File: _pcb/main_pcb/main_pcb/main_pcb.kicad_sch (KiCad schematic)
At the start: 1 part, among them U1 Pico

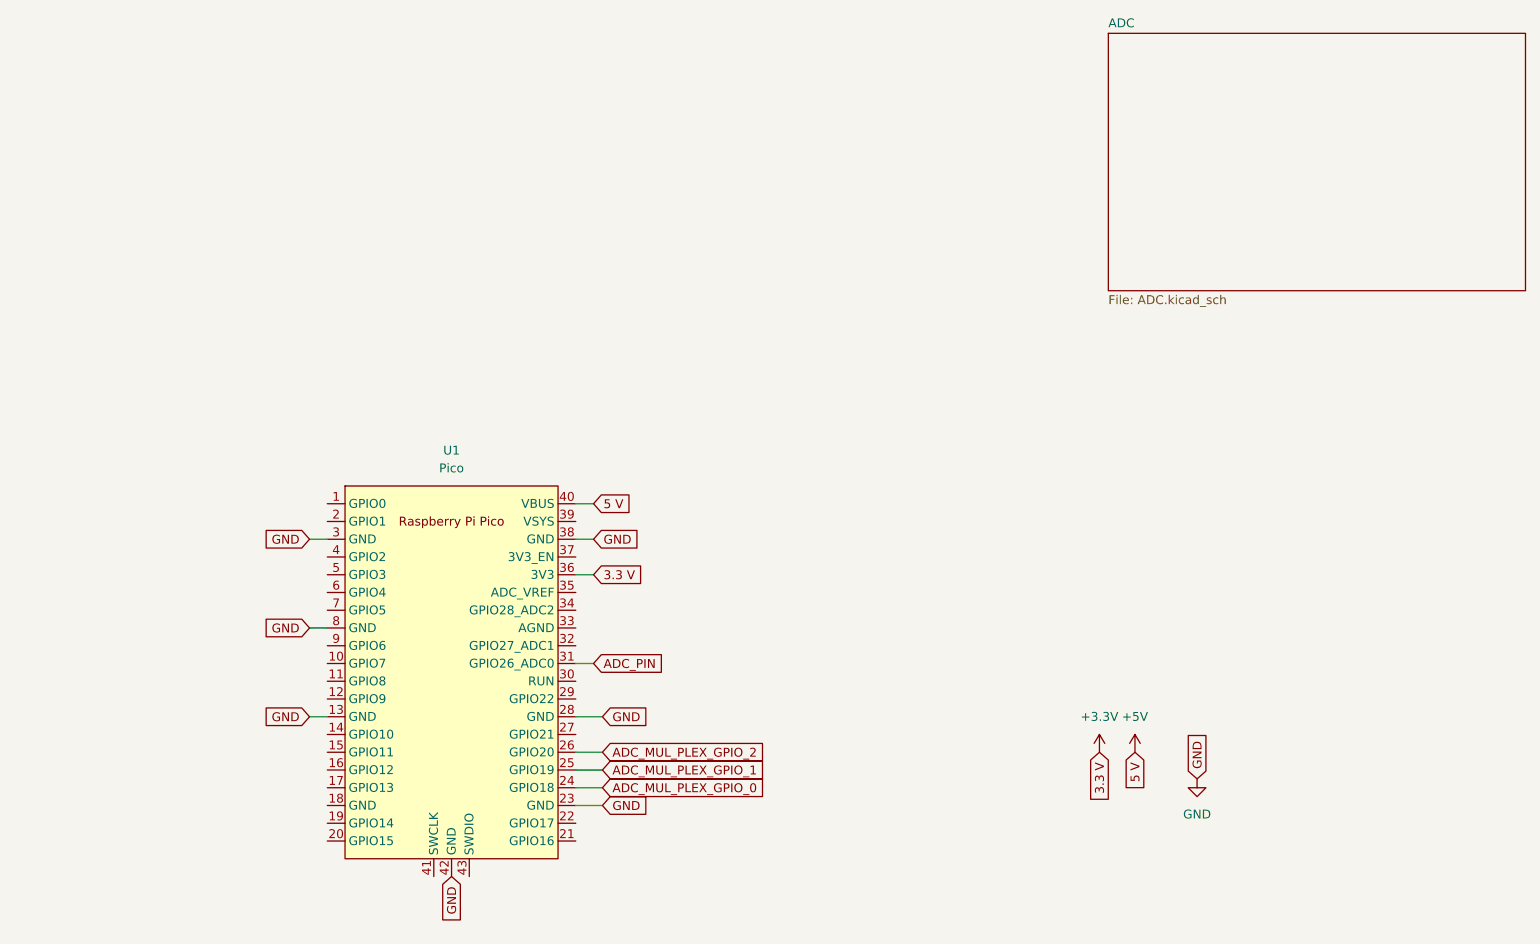
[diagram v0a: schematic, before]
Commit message: added io expander and rotSW only ws2812 missing
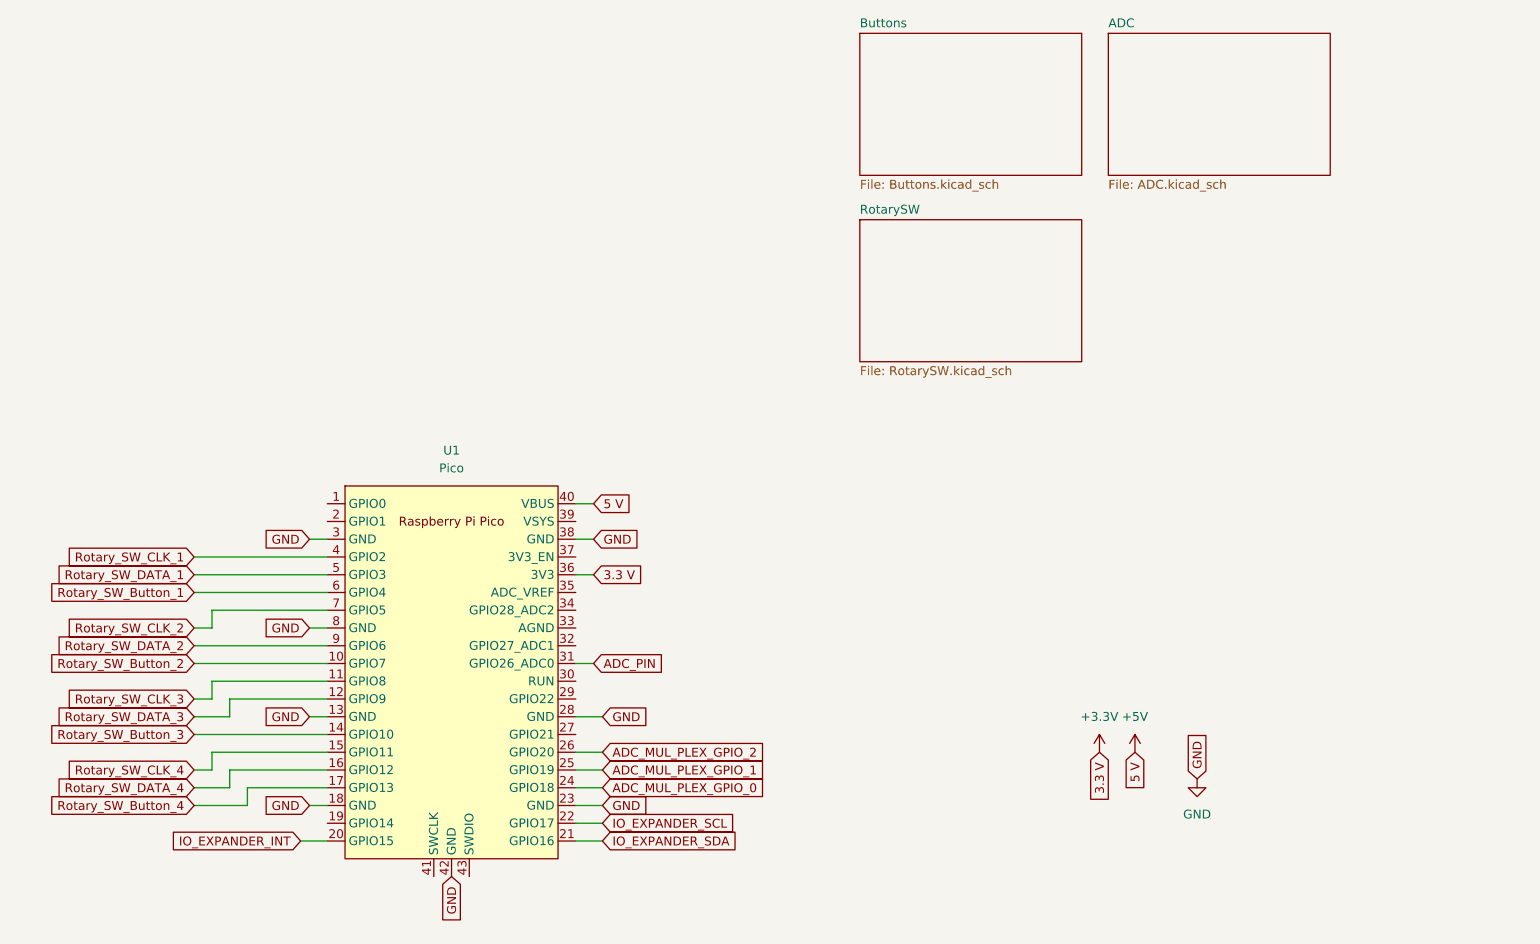
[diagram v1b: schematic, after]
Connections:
- net GND: now also U1.18 (GND)
- net Rotary_SW_Button_2: now reaches U1.10 (GPIO7)
- net Rotary_SW_CLK_3: now reaches U1.11 (GPIO8)
- net Rotary_SW_DATA_3: now reaches U1.12 (GPIO9)
- net Rotary_SW_Button_3: now reaches U1.14 (GPIO10)
- net Rotary_SW_CLK_4: now reaches U1.15 (GPIO11)
- net Rotary_SW_DATA_4: now reaches U1.16 (GPIO12)
- net Rotary_SW_Button_4: now reaches U1.17 (GPIO13)
- net IO_EXPANDER_INT: now reaches U1.20 (GPIO15)
- net IO_EXPANDER_SDA: now reaches U1.21 (GPIO16)
- net IO_EXPANDER_SCL: now reaches U1.22 (GPIO17)
- net Rotary_SW_CLK_1: now reaches U1.4 (GPIO2)
- net Rotary_SW_DATA_1: now reaches U1.5 (GPIO3)
- net Rotary_SW_Button_1: now reaches U1.6 (GPIO4)
- net Rotary_SW_CLK_2: now reaches U1.7 (GPIO5)
- net Rotary_SW_DATA_2: now reaches U1.9 (GPIO6)
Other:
- added sheet Buttons (Buttons.kicad_sch)
- added sheet RotarySW (RotarySW.kicad_sch)

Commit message: added WS2812
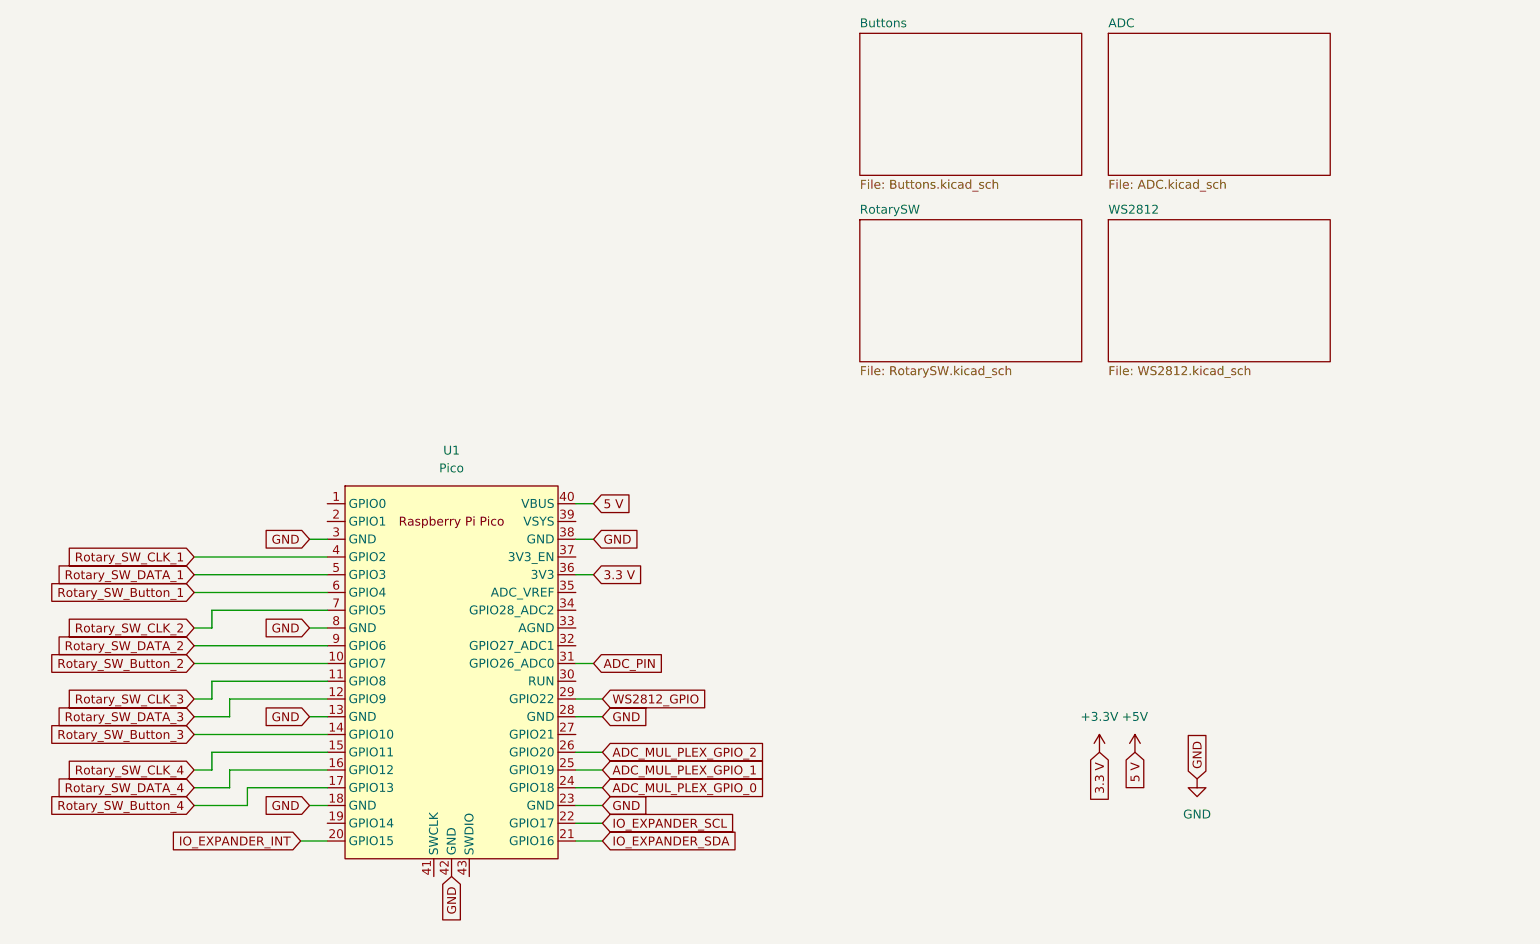
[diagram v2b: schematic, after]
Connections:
- net WS2812_GPIO: now reaches U1.29 (GPIO22)
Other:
- added sheet WS2812 (WS2812.kicad_sch)
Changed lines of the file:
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@@
+	(wire
+		(pts
+			(xy 118.11 134.62) (xy 121.92 134.62)
+		)
+		(stroke
+			(width 0)
+			(type default)
+		)
+	)
 	(wire
 		(pts
@@
 				)
 				(justify right)
+				(hide yes)
+			)
+		)
+	)
+	(global_label "WS2812_GPIO"
+		(shape input)
+		(at 121.92 134.62 0)
+		(fields_autoplaced yes)
+		(effects
+			(font
+				(size 1.27 1.27)
+			)
+			(justify left)
+		)
+		(property "Intersheetrefs" "${INTERSHEET_REFS}"
+			(at 137.847 134.62 0)
+			(effects
+				(font
+					(size 1.27 1.27)
+				)
+				(justify left)
 				(hide yes)
 			)
@@
 				)
 			)
+		)
+	)
+	(sheet
+		(at 194.31 66.04)
+		(size 31.75 20.32)
+		(fields_autoplaced yes)
+		(stroke
+			(width 0.1524)
+			(type solid)
+		)
+		(fill
+			(color 0 0 0 0.0000)
+		)
+		(property "Sheetname" "WS2812"
+			(at 194.31 65.3284 0)
+			(effects
+				(font
+					(size 1.27 1.27)
+				)
+				(justify left bottom)
+			)
+		)
+		(property "Sheetfile" "WS2812.kicad_sch"
+			(at 194.31 86.9446 0)
+			(effects
+				(font
+					(size 1.27 1.27)
+				)
+				(justify left top)
+			)
+		)
+		(instances
+			(project "main_pcb"
+				(path "/b764235d-842d-41df-960a-a32e4258c2ec"
+					(page "5")
+				)
+			)

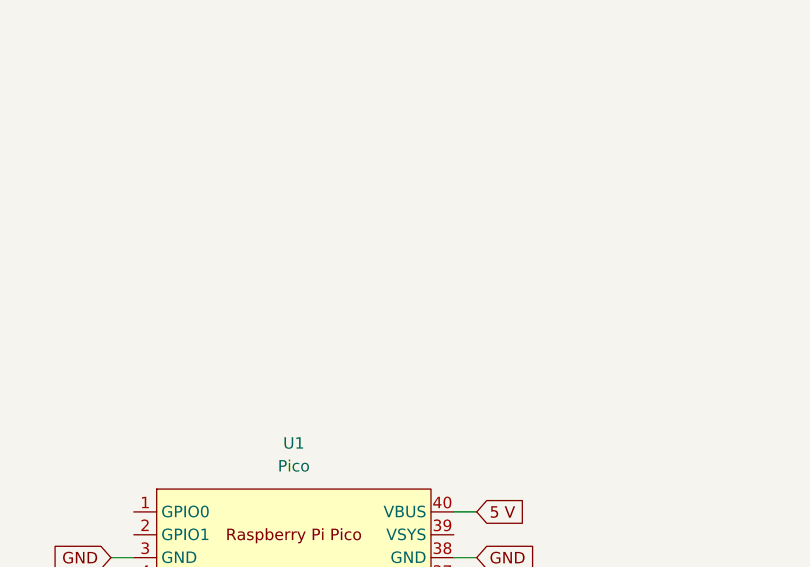
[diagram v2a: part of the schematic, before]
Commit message: for now the last commit for pcb as buying pcb is too expensive
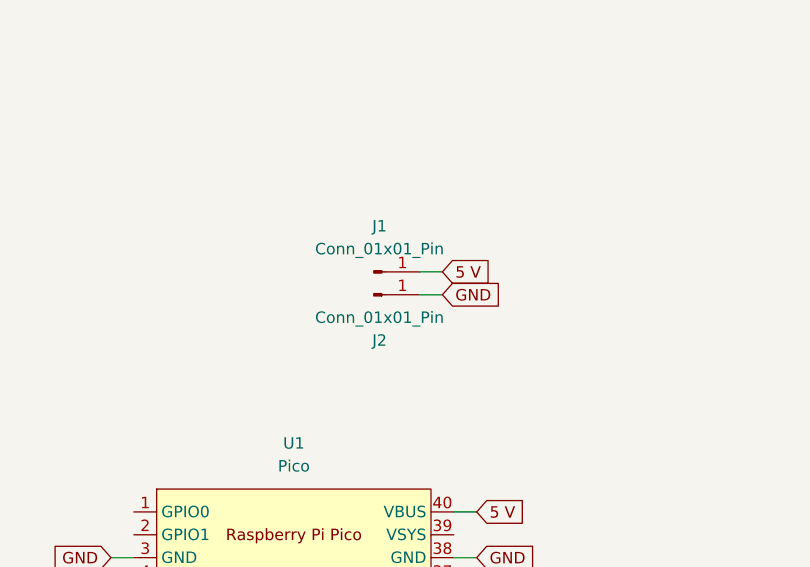
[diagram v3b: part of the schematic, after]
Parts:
- added J1, J2: Conn_01x01_Pin, TestPoint:TestPoint_Pad_3.0x3.0mm, symbol Connector:Conn_01x01_Pin
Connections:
- net +5V: now also J1.1 (Pin_1)
- net GND: now also J2.1 (Pin_1)
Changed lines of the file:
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@@
+	(wire
+		(pts
+			(xy 116.84 82.55) (xy 114.3 82.55)
+		)
+		(stroke
+			(width 0)
+			(type default)
+		)
+	)
 	(wire
 		(pts
@@
 	(wire
 		(pts
+			(xy 116.84 80.01) (xy 114.3 80.01)
+		)
+		(stroke
+			(width 0)
+			(type default)
+		)
+	)
+	(wire
+		(pts
 			(xy 121.92 142.24) (xy 118.11 142.24)
 		)
@@
 		)
 	)
+	(global_label "5 V"
+		(shape input)
+		(at 116.84 80.01 0)
+		(fields_autoplaced yes)
+		(effects
+			(font
+				(size 1.27 1.27)
+			)
+			(justify left)
+		)
+		(property "Intersheetrefs" "${INTERSHEET_REFS}"
+			(at 123.0909 80.01 0)
+			(effects
+				(font
+					(size 1.27 1.27)
+				)
+				(justify left)
+				(hide yes)
+			)
+		)
+	)
 	(global_label "Rotary_SW_CLK_1"
 		(shape input)
@@
 		(property "Intersheetrefs" "${INTERSHEET_REFS}"
 			(at 128.7152 116.84 0)
+			(effects
+				(font
+					(size 1.27 1.27)
+				)
+				(justify left)
+				(hide yes)
+			)
+		)
+	)
+	(global_label "GND"
+		(shape input)
+		(at 116.84 82.55 0)
+		(fields_autoplaced yes)
+		(effects
+			(font
+				(size 1.27 1.27)
+			)
+			(justify left)
+		)
+		(property "Intersheetrefs" "${INTERSHEET_REFS}"
+			(at 123.6957 82.55 0)
 			(effects
 				(font
@@
 					(unit 1)
 				)
+			)
+		)
+	)
+	(symbol
+		(lib_id "Connector:Conn_01x01_Pin")
+		(at 109.22 82.55 0)
+		(mirror x)
+		(unit 1)
+		(exclude_from_sim no)
+		(in_bom yes)
+		(on_board yes)
+		(dnp no)
+		(property "Reference" "J2"
+			(at 109.855 87.63 0)
+			(effects
+				(font
+					(size 1.27 1.27)
+				)
+			)
+		)
+		(property "Value" "Conn_01x01_Pin"
+			(at 109.855 85.09 0)
+			(effects
+				(font
+					(size 1.27 1.27)
+				)
+			)
+		)
+		(property "Footprint" "TestPoint:TestPoint_Pad_3.0x3.0mm"
+			(at 109.22 82.55 0)
+			(effects
+				(font
+					(size 1.27 1.27)
+				)
+				(hide yes)
+			)
+		)
+		(property "Datasheet" "~"
+			(at 109.22 82.55 0)
+			(effects
+				(font
+					(size 1.27 1.27)
+				)
+				(hide yes)
+			)
+		)
+		(property "Description" "Generic connector, single row, 01x01, script generated"
+			(at 109.22 82.55 0)
+			(effects
+				(font
+					(size 1.27 1.27)
+				)
+				(hide yes)
+			)
+		)
+		(pin "1"
+		)
+		(instances
+			(project "main_pcb"
+				(path "/b764235d-842d-41df-960a-a32e4258c2ec"
+					(reference "J2")
+					(unit 1)
+				)
+			)
+		)
+	)
+	(symbol
+		(lib_id "Connector:Conn_01x01_Pin")
+		(at 109.22 80.01 0)
+		(unit 1)
+		(exclude_from_sim no)
+		(in_bom yes)
+		(on_board yes)
+		(dnp no)
+		(fields_autoplaced yes)
+		(property "Reference" "J1"
+			(at 109.855 74.93 0)
+			(effects
+				(font
+					(size 1.27 1.27)
+				)
+			)
+		)
+		(property "Value" "Conn_01x01_Pin"
+			(at 109.855 77.47 0)
+			(effects
+				(font
+					(size 1.27 1.27)
+				)
+			)
+		)
+		(property "Footprint" "TestPoint:TestPoint_Pad_3.0x3.0mm"
+			(at 109.22 80.01 0)
+			(effects
+				(font
+					(size 1.27 1.27)
+				)
+				(hide yes)
+			)
+		)
+		(property "Datasheet" "~"
+			(at 109.22 80.01 0)
+			(effects
+				(font
+					(size 1.27 1.27)
+				)
+				(hide yes)
+			)
+		)
+		(property "Description" "Generic connector, single row, 01x01, script generated"
+			(at 109.22 80.01 0)
+			(effects
+				(font
+					(size 1.27 1.27)
+				)
+				(hide yes)
+			)
+		)
+		(pin "1"
+		)
+		(instances
+			(project ""
+				(path "/b764235d-842d-41df-960a-a32e4258c2ec"
+					(reference "J1")
+					(unit 1)
+				)
